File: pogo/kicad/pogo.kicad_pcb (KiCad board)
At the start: 2 copper layers, 7.6 x 14.4 mm, 7 parts

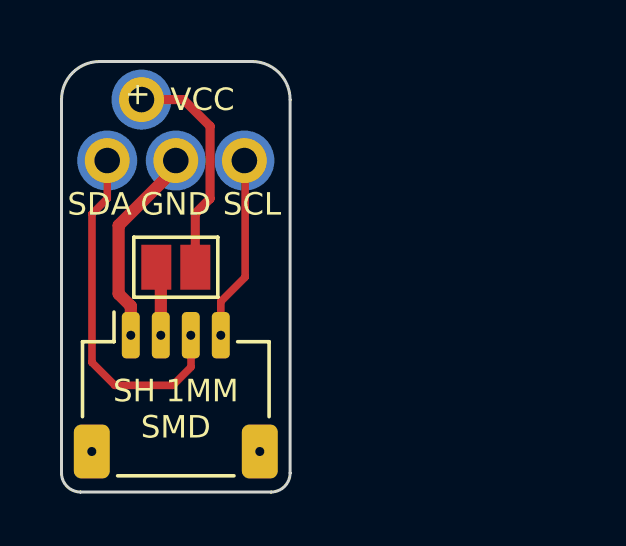
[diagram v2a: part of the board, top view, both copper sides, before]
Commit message: Added pogo socket symbol
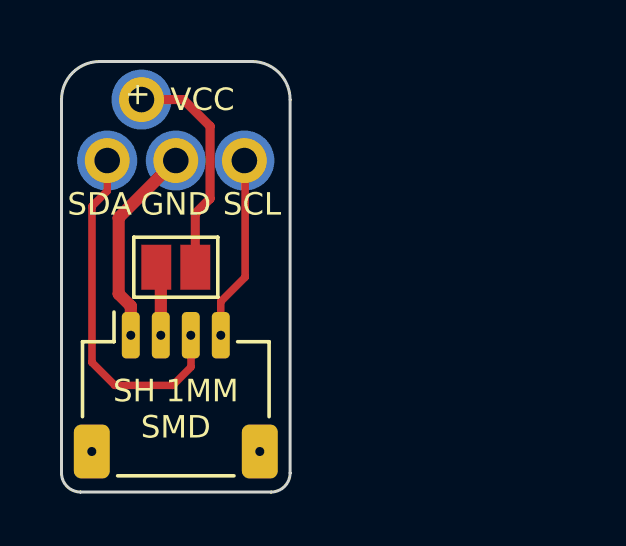
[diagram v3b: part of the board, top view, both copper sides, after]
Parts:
- removed the REF** at (2.29, 0.00)
- removed the REF** at (-1.14, -2.03)
- removed the REF** at (-2.29, 0.00)
- removed the REF** at (0.00, 0.00)
- added REF**: POGO_PINS, pogo:POGO_PINS, F.Cu at (0.00, 0.00)
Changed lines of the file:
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@@
   )
   (net 0 "")
-  (footprint "pogo:POGO_PIN" (layer "F.Cu")
-    (at 2.286 0)
-    (descr "Through hole straight pin header, 1x01, 2.54mm pitch, single row")
-    (tags "Through hole pin header THT 1x01 2.54mm single row")
-    (attr through_hole)
-    (fp_text reference "REF**" (at 0 -2.33) (layer "F.SilkS") hide
-        (effects (font (size 1 1) (thickness 0.15)))
-    )
-    (fp_text value "POGO_PIN" (at 0 2.33) (layer "F.Fab") hide
-        (effects (font (size 1 1) (thickness 0.15)))
-    )
-    (fp_circle (center 0 0) (end 0.85 0)
-      (stroke (width 0.3) (type solid)) (fill none) (layer "B.Cu"))
-    (fp_circle (center 0 0) (end 0.85 0)
-      (stroke (width 0.3) (type solid)) (fill none) (layer "B.Mask"))
-    (pad "1" thru_hole circle (at 0 0) (size 1.5 1.5) (drill 0.85) (layers "*.Cu" "*.Mask"))
-    (model "${KICAD6_3DMODEL_DIR}/Connector_PinHeader_2.54mm.3dshapes/PinHeader_1x01_P2.54mm_Vertical.wrl"
-      (offset (xyz 0 0 0))
-      (scale (xyz 1 1 1))
-      (rotate (xyz 0 0 0))
-    )
-  )
   (footprint "pogo:JST_SH_SM04B-SRSS-TB_1x04-1MP_P1.00mm_Horizontal" (layer "F.Cu")
     (at 0 7.8232)
@@
     )
   )
-  (footprint "pogo:POGO_PIN" (layer "F.Cu")
-    (at -1.143 -2.032)
+  (footprint "pogo:POGO_PINS" (layer "F.Cu")
+    (at 0 0)
     (descr "Through hole straight pin header, 1x01, 2.54mm pitch, single row")
     (tags "Through hole pin header THT 1x01 2.54mm single row")
     (attr through_hole)
-    (fp_text reference "REF**" (at 0 -2.33) (layer "F.SilkS") hide
+    (fp_text reference "REF**" (at 1.016 -4.445) (layer "F.SilkS") hide
         (effects (font (size 1 1) (thickness 0.15)))
     )
-    (fp_text value "POGO_PIN" (at 0 2.33) (layer "F.Fab") hide
+    (fp_text value "POGO_PINS" (at 0 2.33) (layer "F.Fab") hide
         (effects (font (size 1 1) (thickness 0.15)))
     )
+    (fp_circle (center -2.286 0) (end -1.436 0)
+      (stroke (width 0.3) (type solid)) (fill none) (layer "B.Cu"))
+    (fp_circle (center -1.143 -2.032) (end -0.293 -2.032)
+      (stroke (width 0.3) (type solid)) (fill none) (layer "B.Cu"))
     (fp_circle (center 0 0) (end 0.85 0)
       (stroke (width 0.3) (type solid)) (fill none) (layer "B.Cu"))
+    (fp_circle (center 2.286 0) (end 3.136 0)
+      (stroke (width 0.3) (type solid)) (fill none) (layer "B.Cu"))
+    (fp_circle (center -2.286 0) (end -1.436 0)
+      (stroke (width 0.3) (type solid)) (fill none) (layer "B.Mask"))
+    (fp_circle (center -1.143 -2.032) (end -0.293 -2.032)
+      (stroke (width 0.3) (type solid)) (fill none) (layer "B.Mask"))
     (fp_circle (center 0 0) (end 0.85 0)
       (stroke (width 0.3) (type solid)) (fill none) (layer "B.Mask"))
-    (pad "1" thru_hole circle (at 0 0) (size 1.5 1.5) (drill 0.85) (layers "*.Cu" "*.Mask"))
-    (model "${KICAD6_3DMODEL_DIR}/Connector_PinHeader_2.54mm.3dshapes/PinHeader_1x01_P2.54mm_Vertical.wrl"
-      (offset (xyz 0 0 0))
-      (scale (xyz 1 1 1))
-      (rotate (xyz 0 0 0))
-    )
-  )
-  (footprint "pogo:POGO_PIN" (layer "F.Cu")
-    (at -2.286 0)
-    (descr "Through hole straight pin header, 1x01, 2.54mm pitch, single row")
-    (tags "Through hole pin header THT 1x01 2.54mm single row")
-    (attr through_hole)
-    (fp_text reference "REF**" (at 0 -2.33) (layer "F.SilkS") hide
-        (effects (font (size 1 1) (thickness 0.15)))
-    )
-    (fp_text value "POGO_PIN" (at 0 2.33) (layer "F.Fab") hide
-        (effects (font (size 1 1) (thickness 0.15)))
-    )
-    (fp_circle (center 0 0) (end 0.85 0)
-      (stroke (width 0.3) (type solid)) (fill none) (layer "B.Cu"))
-    (fp_circle (center 0 0) (end 0.85 0)
+    (fp_circle (center 2.286 0) (end 3.136 0)
       (stroke (width 0.3) (type solid)) (fill none) (layer "B.Mask"))
-    (pad "1" thru_hole circle (at 0 0) (size 1.5 1.5) (drill 0.85) (layers "*.Cu" "*.Mask"))
+    (pad "1" thru_hole circle (at -2.286 0) (size 1.5 1.5) (drill 0.85) (layers "*.Cu" "*.Mask"))
+    (pad "2" thru_hole circle (at 0 0) (size 1.5 1.5) (drill 0.85) (layers "*.Cu" "*.Mask"))
+    (pad "3" thru_hole circle (at 2.286 0) (size 1.5 1.5) (drill 0.85) (layers "*.Cu" "*.Mask"))
+    (pad "4" thru_hole circle (at -1.143 -2.032) (size 1.5 1.5) (drill 0.85) (layers "*.Cu" "*.Mask"))
     (model "${KICAD6_3DMODEL_DIR}/Connector_PinHeader_2.54mm.3dshapes/PinHeader_1x01_P2.54mm_Vertical.wrl"
       (offset (xyz 0 0 0))
@@
     (pad "1" smd rect (at -0.65 0) (size 1 1.5) (layers "F.Cu" "F.Mask"))
     (pad "2" smd rect (at 0.65 0) (size 1 1.5) (layers "F.Cu" "F.Mask"))
-  )
-  (footprint "pogo:POGO_PIN" (layer "F.Cu")
-    (at 0 0)
-    (descr "Through hole straight pin header, 1x01, 2.54mm pitch, single row")
-    (tags "Through hole pin header THT 1x01 2.54mm single row")
-    (attr through_hole)
-    (fp_text reference "REF**" (at 0 -2.33) (layer "F.SilkS") hide
-        (effects (font (size 1 1) (thickness 0.15)))
-    )
-    (fp_text value "POGO_PIN" (at 0 2.33) (layer "F.Fab") hide
-        (effects (font (size 1 1) (thickness 0.15)))
-    )
-    (fp_circle (center 0 0) (end 0.85 0)
-      (stroke (width 0.3) (type solid)) (fill none) (layer "B.Cu"))
-    (fp_circle (center 0 0) (end 0.85 0)
-      (stroke (width 0.3) (type solid)) (fill none) (layer "B.Mask"))
-    (pad "1" thru_hole circle (at 0 0) (size 1.5 1.5) (drill 0.85) (layers "*.Cu" "*.Mask"))
-    (model "${KICAD6_3DMODEL_DIR}/Connector_PinHeader_2.54mm.3dshapes/PinHeader_1x01_P2.54mm_Vertical.wrl"
-      (offset (xyz 0 0 0))
-      (scale (xyz 1 1 1))
-      (rotate (xyz 0 0 0))
-    )
   )
   (gr_arc (start 2.54 -3.302) (mid 3.438026 -2.930026) (end 3.81 -2.032)
@@
   )
   (segment (start 1.143 -1.143) (end 0.254 -2.032) (width 0.3048) (layer "F.Cu") (net 0))
-  (segment (start -1.905 4.445) (end -1.905 2.159) (width 0.4064) (layer "F.Cu") (net 0))
-  (segment (start -1.5 5.62) (end -1.5 4.85) (width 0.4064) (layer "F.Cu") (net 0))
+  (segment (start -1.905 1.905) (end 0 0) (width 0.4064) (layer "F.Cu") (net 0))
   (segment (start -0.65 3.175) (end -0.5 3.325) (width 0.4064) (layer "F.Cu") (net 0))
-  (segment (start -1.5 4.85) (end -1.905 4.445) (width 0.4064) (layer "F.Cu") (net 0))
-  (segment (start -2.286 1.27) (end -2.286 0) (width 0.254) (layer "F.Cu") (net 0))
   (segment (start -0.5 3.325) (end -0.5 5.62) (width 0.4064) (layer "F.Cu") (net 0))
   (segment (start 1.5 5.62) (end 1.5 4.6976) (width 0.254) (layer "F.Cu") (net 0))
@@
   (segment (start 2.3114 0.0254) (end 2.286 0) (width 0.254) (layer "F.Cu") (net 0))
   (segment (start 0.508 6.8834) (end -0.1016 7.493) (width 0.254) (layer "F.Cu") (net 0))
-  (segment (start 0 0.254) (end 0 0) (width 0.4064) (layer "F.Cu") (net 0))
+  (segment (start -2.794 1.524) (end -2.286 1.016) (width 0.254) (layer "F.Cu") (net 0))
+  (segment (start -2.032 7.493) (end -2.794 6.731) (width 0.254) (layer "F.Cu") (net 0))
   (segment (start 0.65 3.175) (end 0.65 1.763) (width 0.3048) (layer "F.Cu") (net 0))
-  (segment (start -1.905 2.159) (end 0 0.254) (width 0.4064) (layer "F.Cu") (net 0))
-  (segment (start -2.794 6.731) (end -2.794 1.778) (width 0.254) (layer "F.Cu") (net 0))
+  (segment (start -1.5 4.85) (end -1.905 4.445) (width 0.4064) (layer "F.Cu") (net 0))
+  (segment (start -2.286 1.016) (end -2.286 0) (width 0.254) (layer "F.Cu") (net 0))
+  (segment (start 0.65 1.763) (end 1.143 1.27) (width 0.3048) (layer "F.Cu") (net 0))
   (segment (start -0.1016 7.493) (end -2.032 7.493) (width 0.254) (layer "F.Cu") (net 0))
-  (segment (start 0.65 1.763) (end 1.143 1.27) (width 0.3048) (layer "F.Cu") (net 0))
-  (segment (start -2.032 7.493) (end -2.794 6.731) (width 0.254) (layer "F.Cu") (net 0))
-  (segment (start -2.794 1.778) (end -2.286 1.27) (width 0.254) (layer "F.Cu") (net 0))
+  (segment (start -1.905 4.445) (end -1.905 1.905) (width 0.4064) (layer "F.Cu") (net 0))
   (segment (start 1.5 4.6976) (end 2.3114 3.8862) (width 0.254) (layer "F.Cu") (net 0))
   (segment (start 2.3114 3.8862) (end 2.3114 0.0254) (width 0.254) (layer "F.Cu") (net 0))
   (segment (start 1.143 1.27) (end 1.143 -1.143) (width 0.3048) (layer "F.Cu") (net 0))
+  (segment (start -1.5 5.62) (end -1.5 4.85) (width 0.4064) (layer "F.Cu") (net 0))
   (segment (start 0.254 -2.032) (end -1.143 -2.032) (width 0.3048) (layer "F.Cu") (net 0))
+  (segment (start -2.794 6.731) (end -2.794 1.524) (width 0.254) (layer "F.Cu") (net 0))
 )

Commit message: More progress with the Pogo layout.
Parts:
- added G*: LOGO, pogo:QWIIC_logo_6mm, B.Cu at (0.04, 4.73)
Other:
- board text added: "NOTE: This PCB layout is not tied to a Kicad schematic."
- board text added: "V0.1"
- board text added: "locked"
- board text removed: "GND"
- board text removed: "POGO PINS THIS SIDE"
- board text removed: "SCL"
- board text removed: "SDA"
- board text removed: "SH 1MM SMD"
- board text removed: "VCC"
